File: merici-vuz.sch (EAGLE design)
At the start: 52 parts, among them IC1 MEGA328-PB, IC2 MCP73831, IC3 LE33, Q1 3,6864 MHz, Q4 TSM2302CX, T1 IRF7306

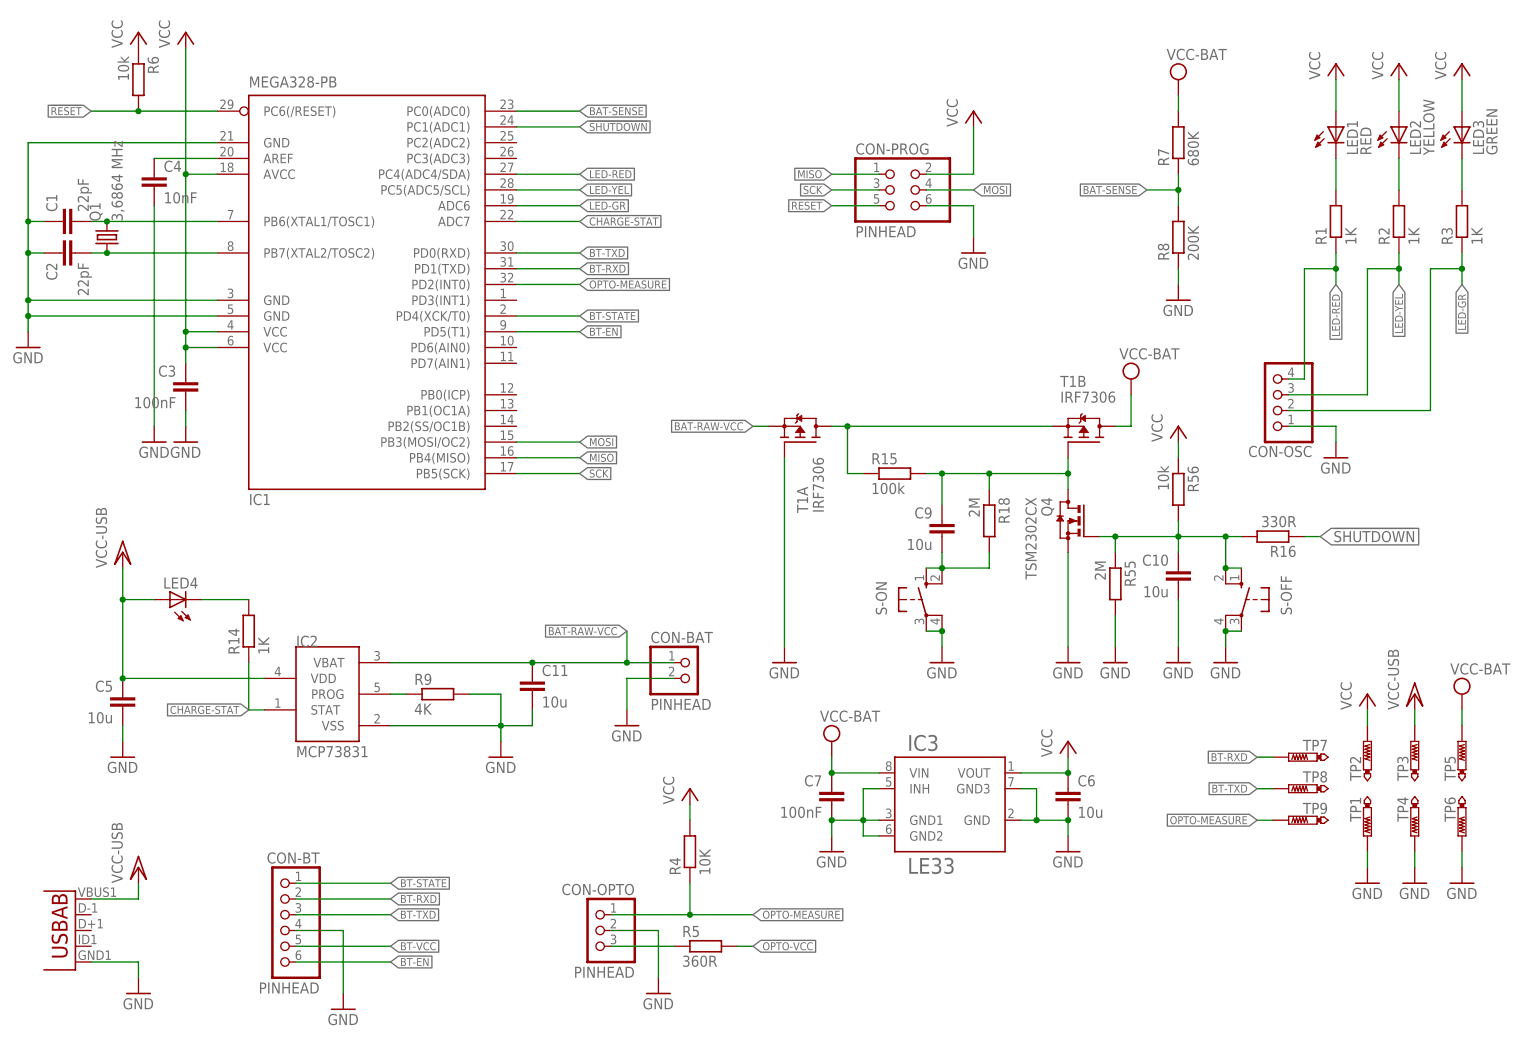
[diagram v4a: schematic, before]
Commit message: Add missing wires & edit debug connector.
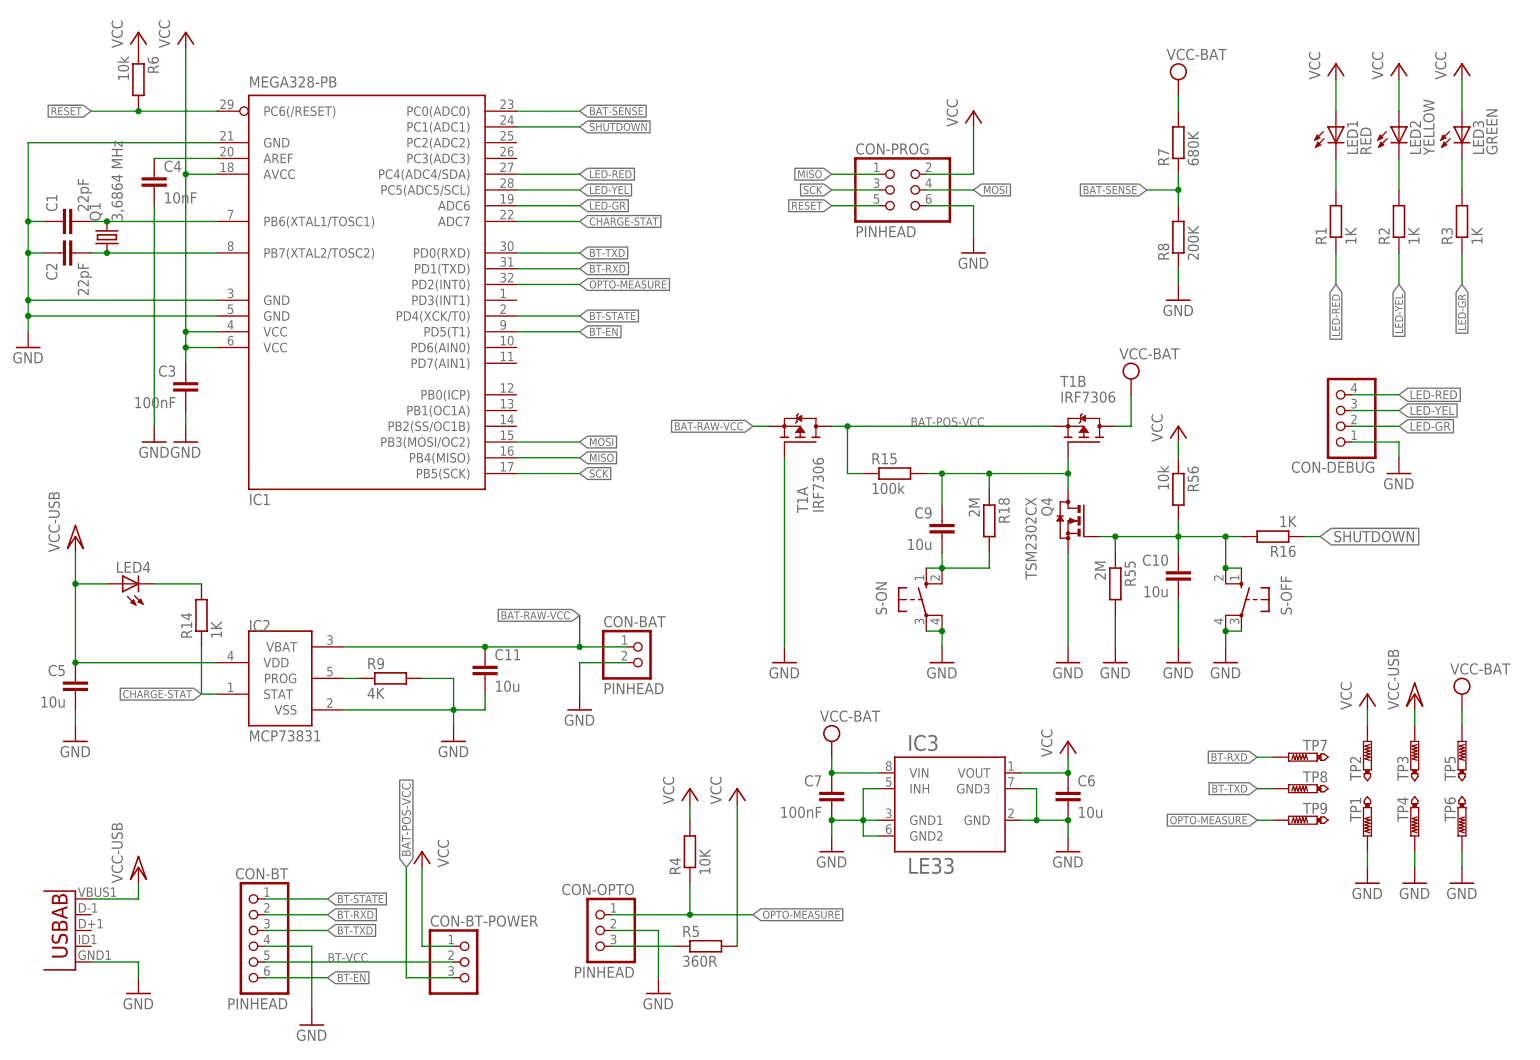
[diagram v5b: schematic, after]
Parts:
- removed CON-OSC: (no value), pinhead:PINHD-1X4
- added CON-BT-POWER: (no value), pinhead:PINHD-1X3
- added CON-DEBUG: (no value), pinhead:PINHD-1X4
- R16: value 330R -> 1K
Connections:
- removed net BAT-TRUE-VCC: R15.1, T1A.D, T1B.S
- removed net OPTO-VCC: R5.2
- new net BAT-POS-VCC: CON-BT-POWER.3, R15.1, T1A.D, T1B.S
- net BT-VCC: now also CON-BT-POWER.2
- net GND: now also CON-DEBUG.1; no longer CON-OSC.1
- net LED-GR: now also CON-DEBUG.2; no longer CON-OSC.2
- net LED-RED: now also CON-DEBUG.4; no longer CON-OSC.4
- net LED-YEL: now also CON-DEBUG.3; no longer CON-OSC.3
- net VCC: now also CON-BT-POWER.1, R5.2; no longer T1B.D
- net VCC-BAT: now also T1B.D
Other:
- note added: "Main board"
- moved on the sheet: C11, C5, CON-BAT, CON-BT, IC2, LED4, R14, R9

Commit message: Add names to signals.
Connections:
- net N$1 renamed CR1
- net N$10 renamed LED-GR-R
- net N$2 renamed CR2
- net N$3 renamed OPTO-VCC
- net N$4 renamed CPU-REF
- net N$5 renamed CHARGE-PROG
- net N$6 renamed CHARGE-STAT-LED
- net N$8 renamed LED-RED-R
- net N$9 renamed LED-YEL-R
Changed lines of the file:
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@@
 </busses>
 <nets>
-<net name="N$1" class="0">
+<net name="CR1" class="0">
 <segment>
 <pinref part="IC1" gate="G$1" pin="PB6(XTAL1/TOSC1)"/>
@@
 </segment>
 </net>
-<net name="N$2" class="0">
+<net name="CR2" class="0">
 <segment>
 <pinref part="C2" gate="G$1" pin="2"/>
@@
 </segment>
 </net>
-<net name="N$8" class="0">
+<net name="LED-RED-R" class="0">
 <segment>
 <pinref part="R1" gate="G$1" pin="2"/>
@@
 </segment>
 </net>
-<net name="N$9" class="0">
+<net name="LED-YEL-R" class="0">
 <segment>
 <pinref part="R2" gate="G$1" pin="2"/>
@@
 </segment>
 </net>
-<net name="N$10" class="0">
+<net name="LED-GR-R" class="0">
 <segment>
 <pinref part="R3" gate="G$1" pin="2"/>
@@
 </segment>
 </net>
-<net name="N$3" class="0">
+<net name="OPTO-VCC" class="0">
 <segment>
 <pinref part="CON-OPTO" gate="A" pin="3"/>
@@
 </segment>
 </net>
-<net name="N$4" class="0">
+<net name="CPU-REF" class="0">
 <segment>
 <pinref part="C4" gate="G$1" pin="1"/>
@@
 </segment>
 </net>
-<net name="N$5" class="0">
+<net name="CHARGE-PROG" class="0">
 <segment>
 <pinref part="R9" gate="G$1" pin="1"/>
@@
 </segment>
 </net>
-<net name="N$6" class="0">
+<net name="CHARGE-STAT-LED" class="0">
 <segment>
 <pinref part="R14" gate="G$1" pin="2"/>

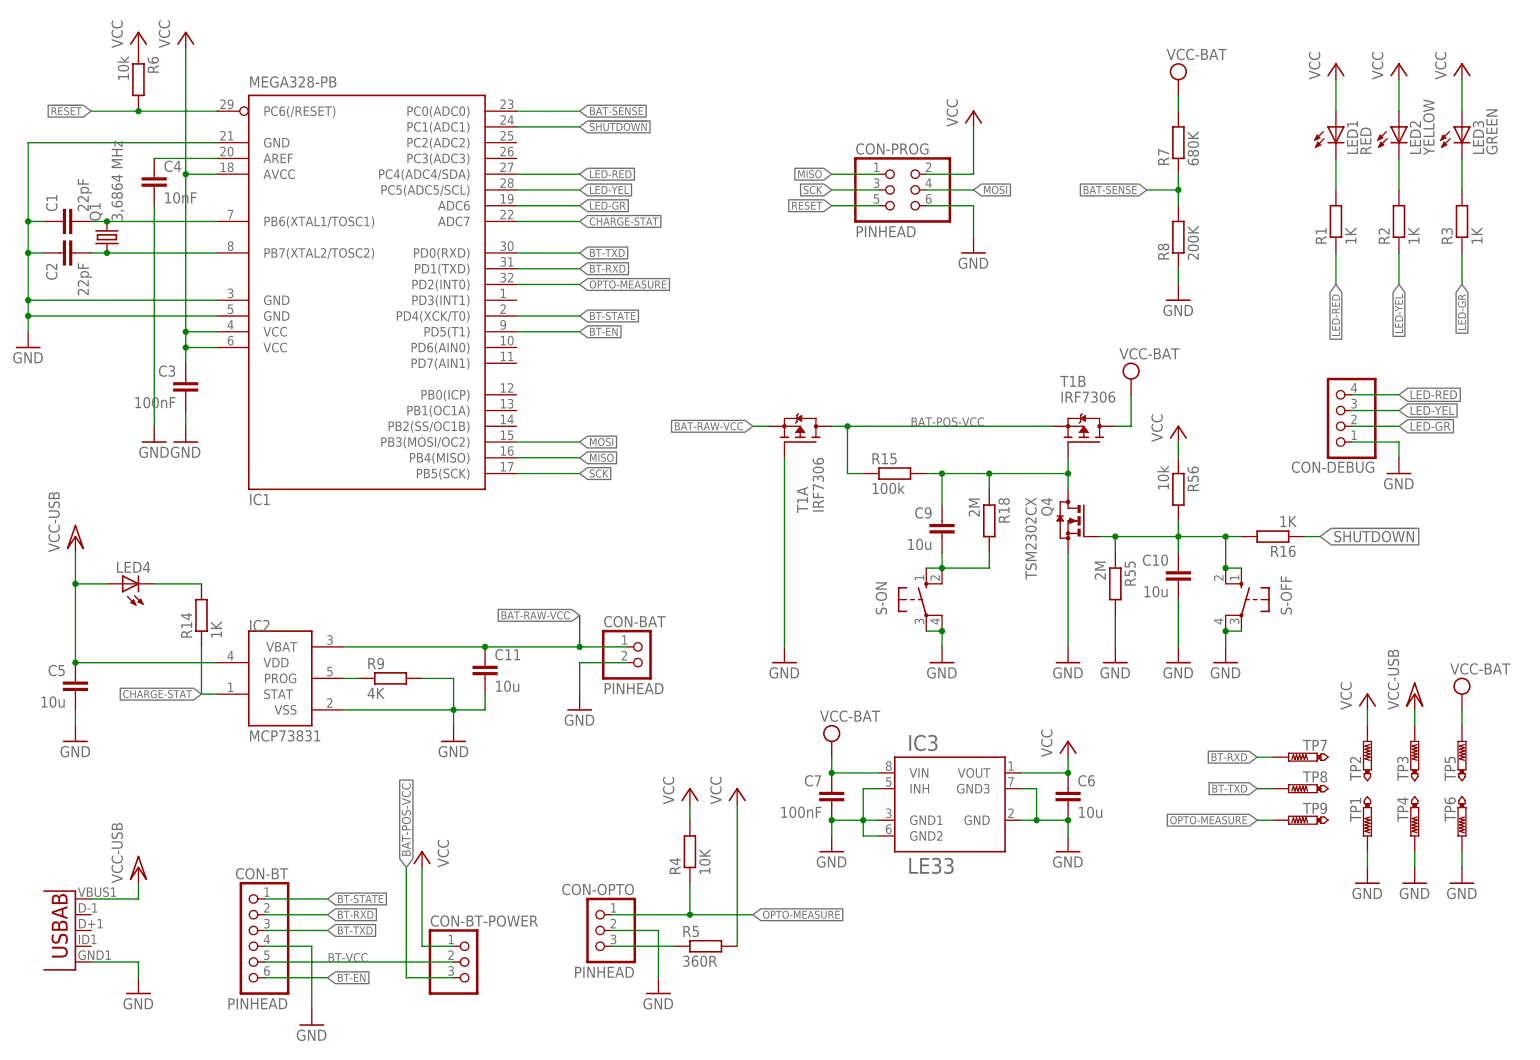
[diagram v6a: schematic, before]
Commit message: Unify names of resistors & capacitors.
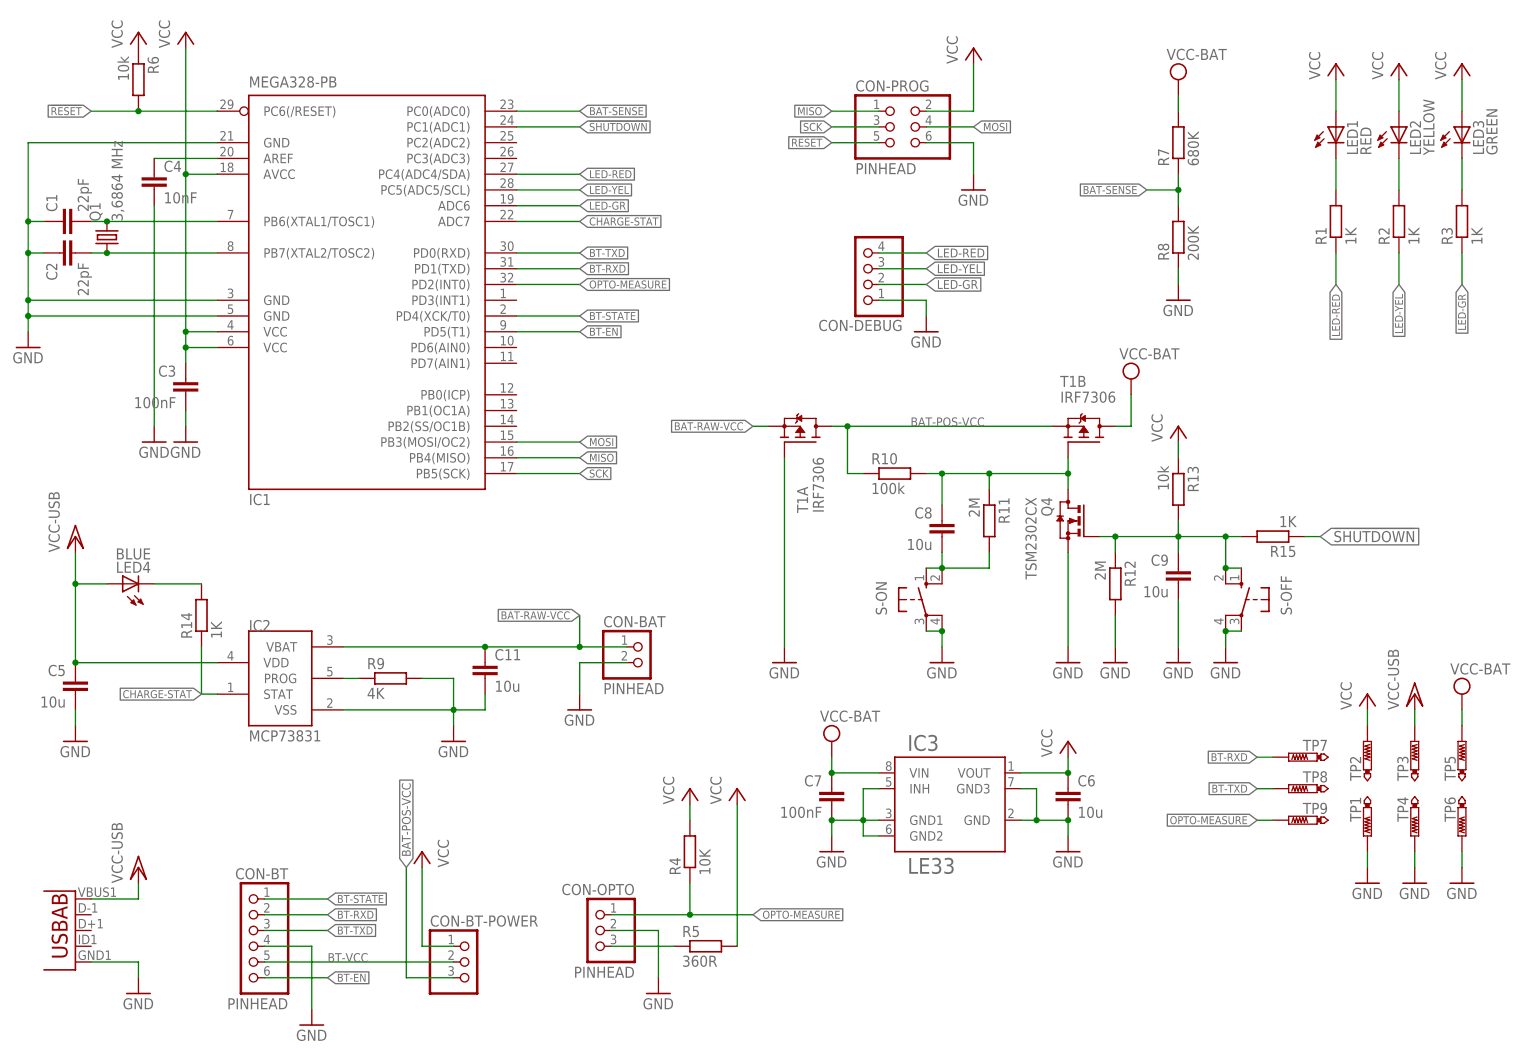
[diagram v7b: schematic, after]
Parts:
- removed C10: 10u, rcl:C-EUC0805
- removed R16: 1K, rcl:R-EU_R0805
- added C8: 10u, rcl:C-EUC0805
- added R10: 100k, rcl:R-EU_R0805
- LED4: value (none) -> BLUE
- R15: value 100k -> 1K
- renumbered R18 to R11, R55 to R12, R56 to R13
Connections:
- net !SHUTDOWN: now also R15.1; no longer R16.1
- net !SHUTDOWN_INT: now also C9.1, R15.2; no longer C10.1, R16.2
- net BAT-POS-VCC: now also R10.1; no longer R15.1
- net GND: now also C9.2; no longer C10.2
- net START_BUTTON: now also C8.2; no longer C9.2
- net START_GATE: now also C8.1, R10.2; no longer C9.1, R15.2
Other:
- moved on the sheet: C9, CON-DEBUG, CON-PROG, R15

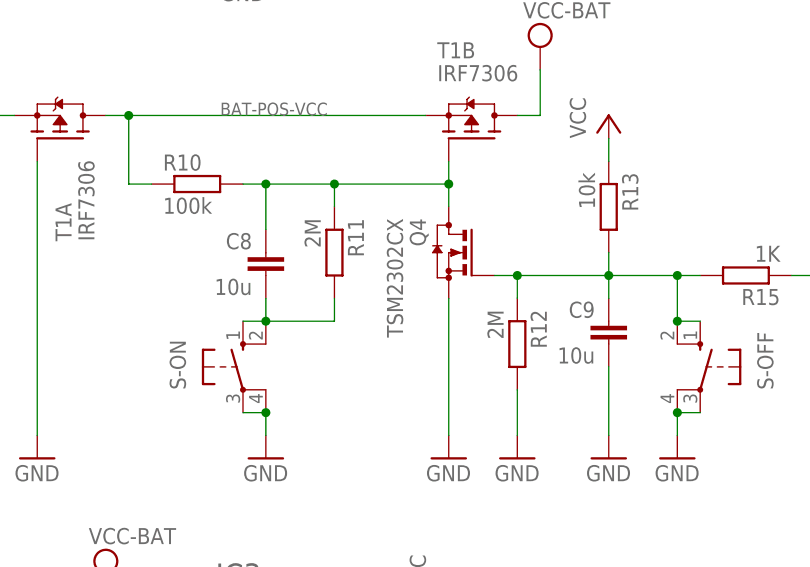
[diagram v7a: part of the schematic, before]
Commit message: Faster on & off switches.
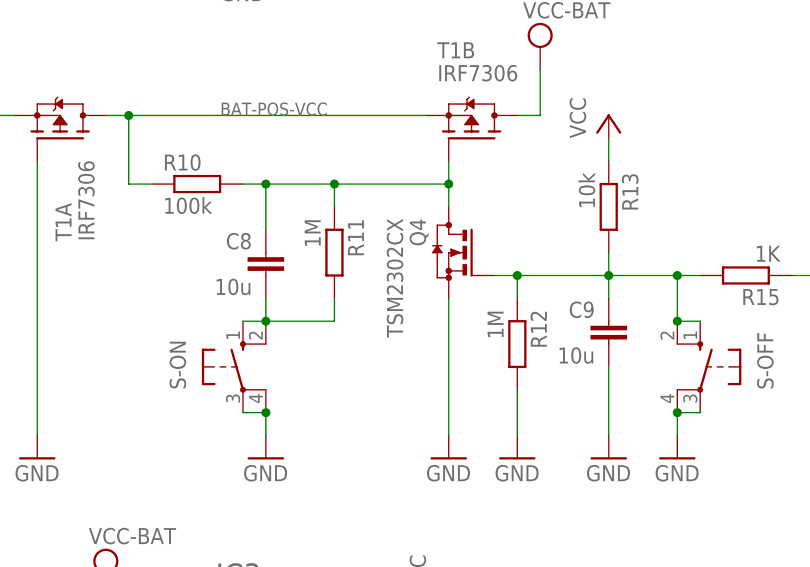
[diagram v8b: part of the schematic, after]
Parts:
- R11, R12: value 2M -> 1M
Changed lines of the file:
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@@
 <part name="R14" library="rcl" deviceset="R-EU_" device="R0805" value="1K"/>
 <part name="C8" library="rcl" deviceset="C-EU" device="C0805" value="10u"/>
-<part name="R12" library="rcl" deviceset="R-EU_" device="R0805" value="2M"/>
+<part name="R12" library="rcl" deviceset="R-EU_" device="R0805" value="1M"/>
 <part name="R13" library="rcl" deviceset="R-EU_" device="R0805" value="10k"/>
 <part name="C9" library="rcl" deviceset="C-EU" device="C0805" value="10u"/>
@@
 <part name="GND49" library="supply1" library_urn="urn:adsk.eagle:library:371" deviceset="GND" device=""/>
 <part name="GND50" library="supply1" library_urn="urn:adsk.eagle:library:371" deviceset="GND" device=""/>
-<part name="R11" library="rcl" deviceset="R-EU_" device="R0805" value="2M"/>
+<part name="R11" library="rcl" deviceset="R-EU_" device="R0805" value="1M"/>
 <part name="GND51" library="supply1" library_urn="urn:adsk.eagle:library:371" deviceset="GND" device=""/>
 <part name="GND52" library="supply1" library_urn="urn:adsk.eagle:library:371" deviceset="GND" device=""/>
